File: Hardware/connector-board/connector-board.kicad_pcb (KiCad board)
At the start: 2 copper layers, 25 x 25 mm, 5 parts, among them J1 Conn_01x06_Pin, J2 Conn_01x06_Pin, J3 Conn_01x06_Pin, J4 Conn_01x06_Pin, J5 Conn_01x10_Pin

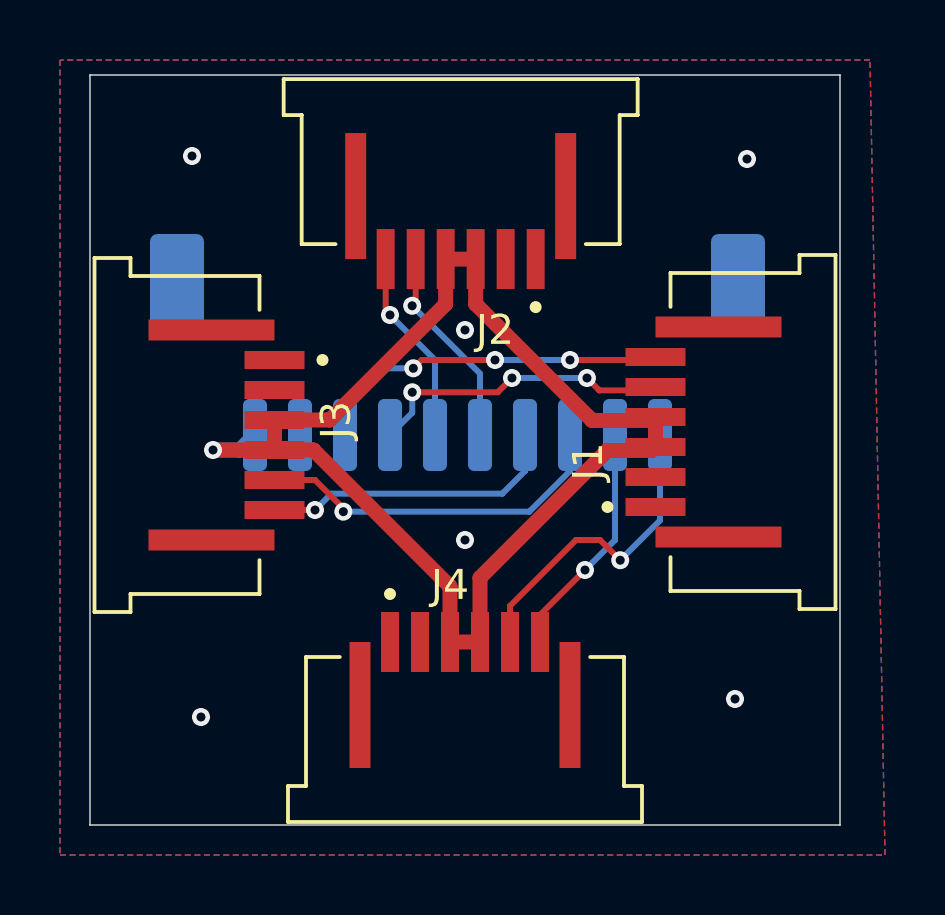
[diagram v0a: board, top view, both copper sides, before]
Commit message: add mounting holes to connector board
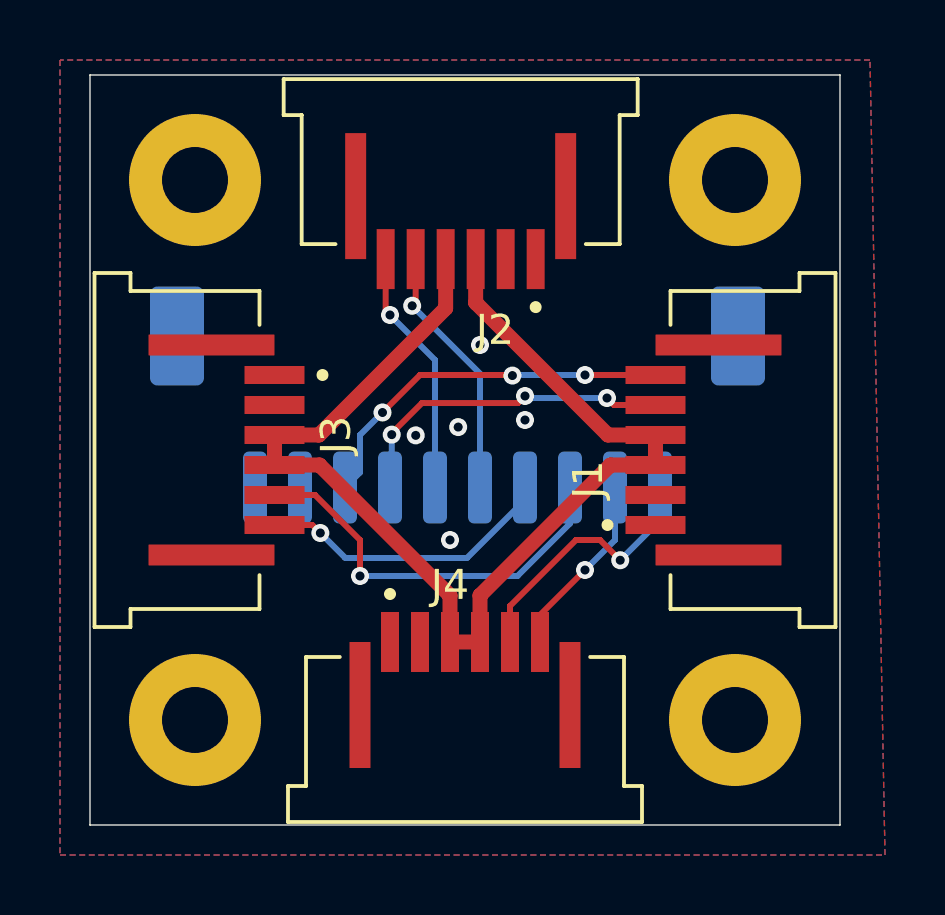
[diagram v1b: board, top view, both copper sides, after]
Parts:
- added H1: MountingHole_Pad, MountingHole:MountingHole_2.2mm_M2_Pad, F.Cu at (152.5, 114.0)
- added H2: MountingHole_Pad, MountingHole:MountingHole_2.2mm_M2_Pad, F.Cu at (170.5, 114.0)
- added H3: MountingHole_Pad, MountingHole:MountingHole_2.2mm_M2_Pad, F.Cu at (152.5, 132.0)
- added H4: MountingHole_Pad, MountingHole:MountingHole_2.2mm_M2_Pad, F.Cu at (170.5, 132.0)
- moved J5 1.75 mm to (161.2, 121.5)
- moved J1 0.60 mm to (171.1, 123.0)
- moved J3 0.50 mm to (151.9, 123.0)
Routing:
- net +3.3V: track 45.0 -> 39.8 mm, vias 1 -> 0
- net FIN4_TX: track 7.94 -> 6.19 mm
- net FIN4_RX: track 10.8 -> 9.04 mm
- net FIN2_TX: track 6.54 -> 8.29 mm
- net FIN2_RX: track 6.85 -> 8.60 mm
- net FIN3_RX: track 12.2 -> 13.6 mm
- net FIN1_RX: track 10.3 -> 11.3 mm
- net FIN1_TX: track 12.1 -> 12.7 mm
- net GND: vias 6 -> 5
